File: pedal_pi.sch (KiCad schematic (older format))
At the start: 20 parts

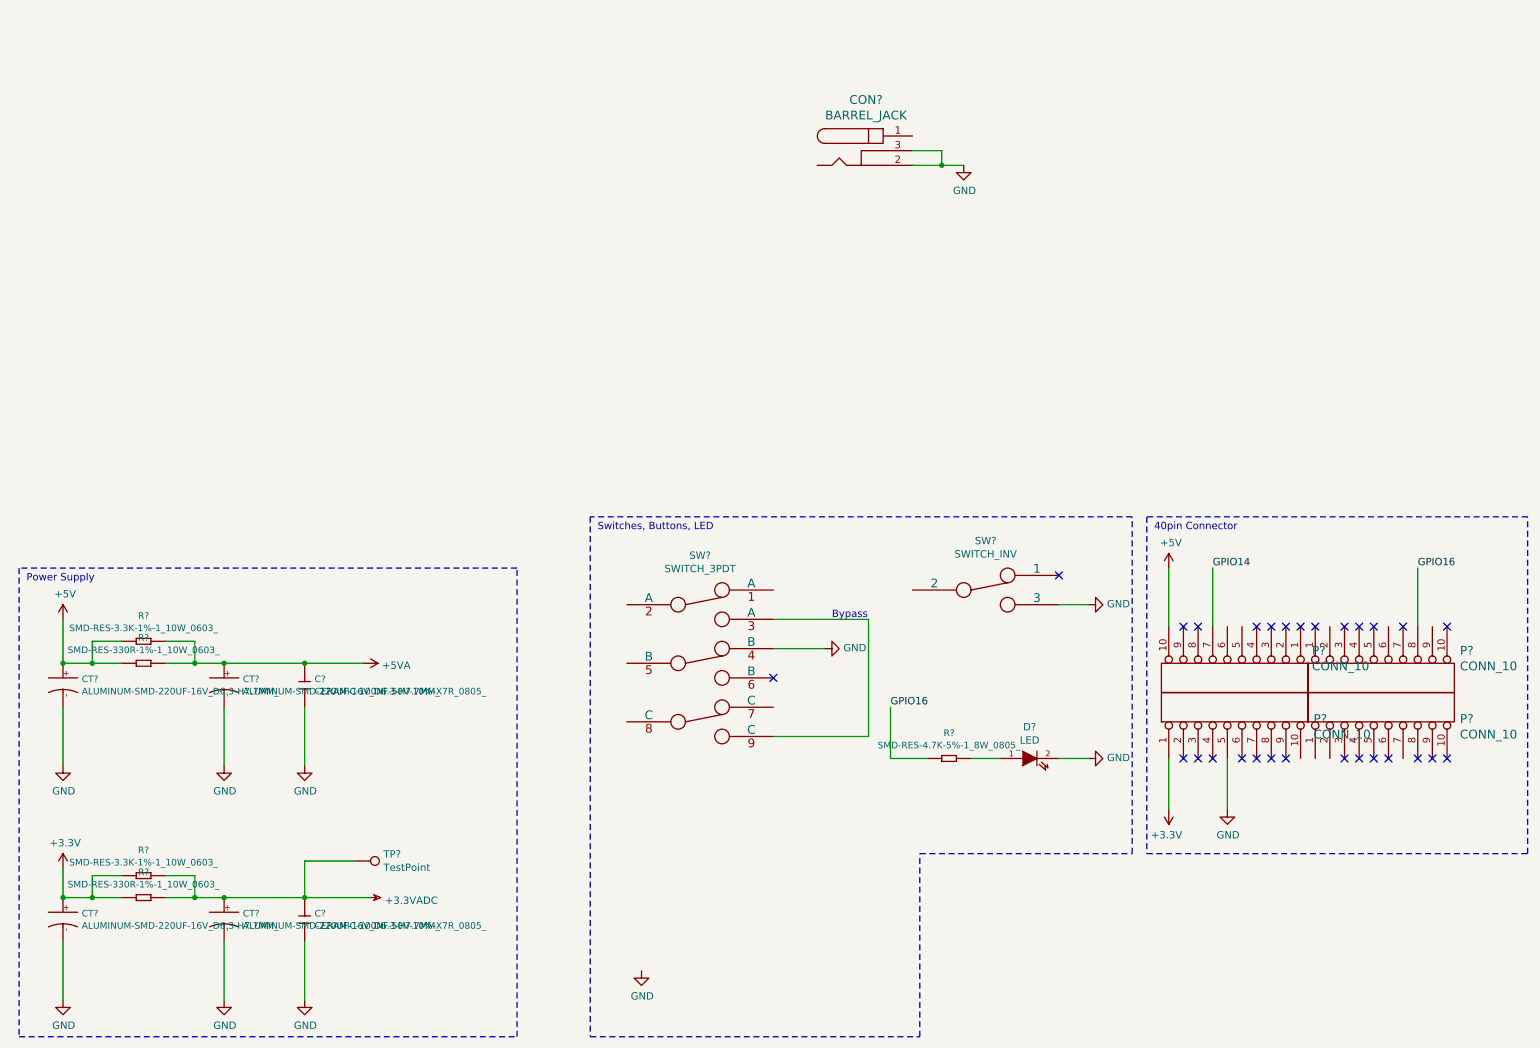
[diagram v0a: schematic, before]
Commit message: added more components to schematic, but stuck on what component to use for dipole ceramic capacitor. List of components that has to be self sourced is placed in the README.md
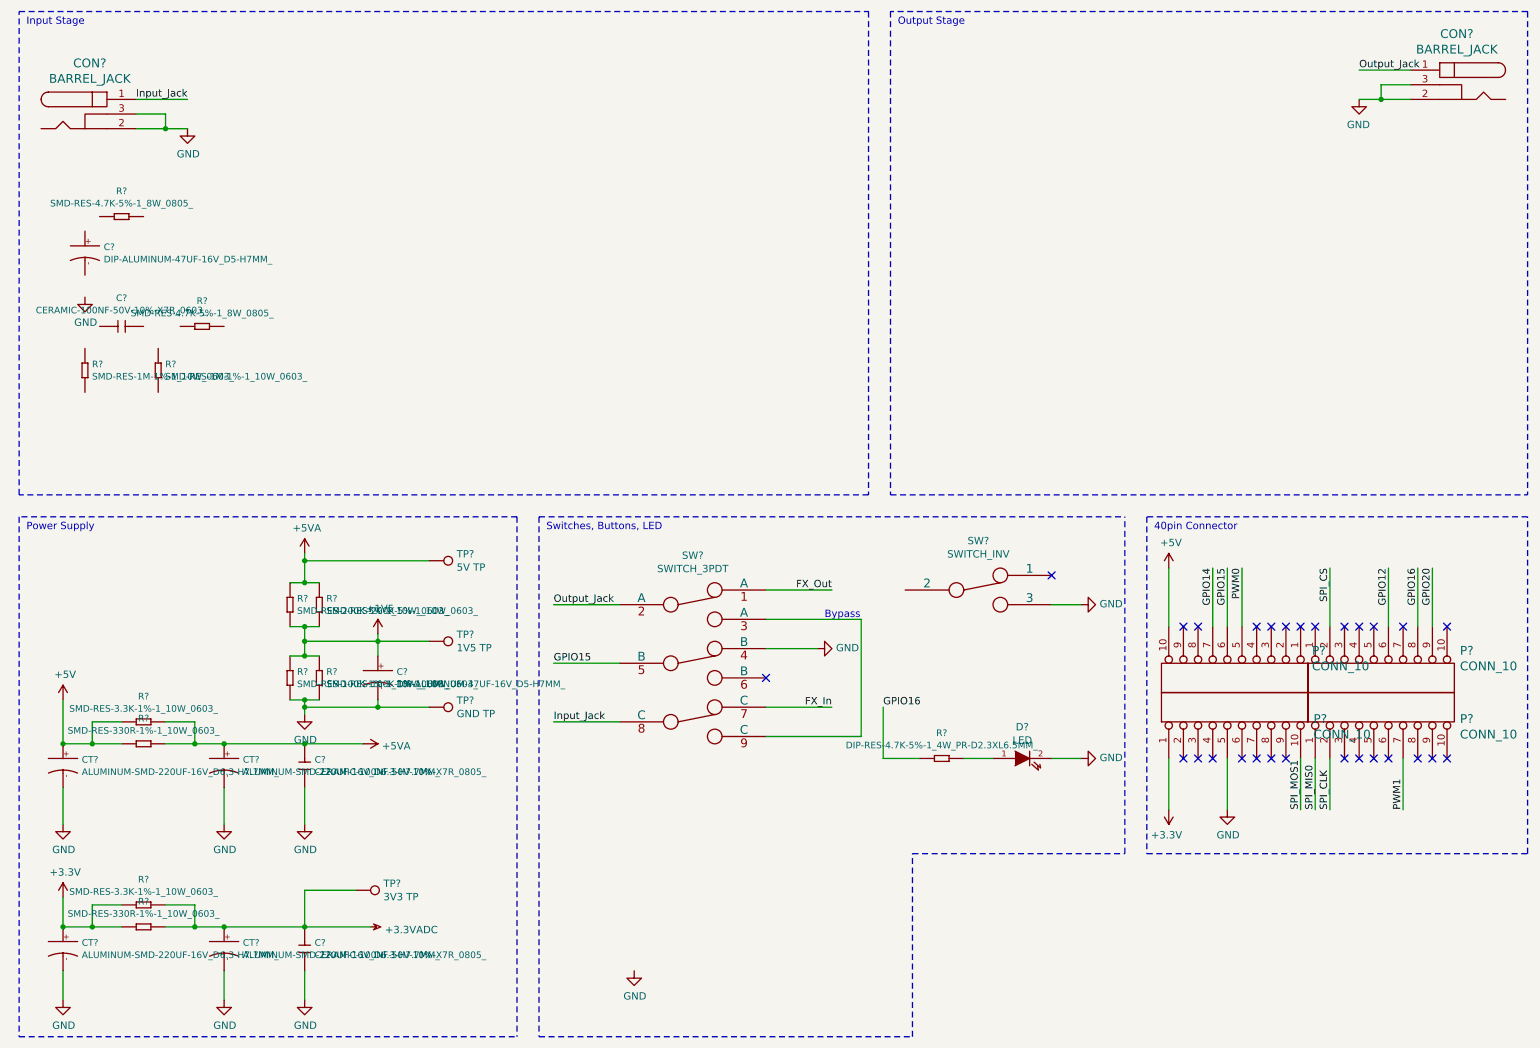
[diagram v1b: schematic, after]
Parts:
- removed R?: SMD-RES-4.7K-5%-1_8W_0805_, symbol OPL_Resistor:SMD-RES-4.7K-5%-1_8W_0805_
- added C?: CERAMIC-100NF-50V-10%-X7R_0603_, symbol OPL_Capacitor:CERAMIC-100NF-50V-10%-X7R_0603_
- added C? (x2): DIP-ALUMINUM-47UF-16V_D5-H7MM_, symbol OPL_Capacitor:DIP-ALUMINUM-47UF-16V_D5-H7MM_
- added CON?: BARREL_JACK, symbol pedal-pi-libs:BARREL_JACK
- added R?: DIP-RES-4.7K-5%-1_4W_PR-D2.3XL6.5MM_, symbol OPL_Resistor:DIP-RES-4.7K-5%-1_4W_PR-D2.3XL6.5MM_
- added R? (x2): SMD-RES-1M-1%-1_10W_0603_, symbol OPL_Resistor:SMD-RES-1M-1%-1_10W_0603_
- added R? (x2): SMD-RES-4.7K-5%-1_8W_0805_, symbol OPL_Resistor:SMD-RES-4.7K-5%-1_8W_0805_
- added R? (x2): SMD-RES-100K-1%-1_10W_0603_, symbol OPL_Resistor:SMD-RES-100K-1%-1_10W_0603_
- added R? (x2): SMD-RES-200K-5%-1_10W_0603_, symbol OPL_Resistor:SMD-RES-200K-5%-1_10W_0603_
- added TP?: 1V5 TP, symbol Connector:TestPoint
- added TP?: GND TP, symbol Connector:TestPoint
- added TP?: 5V TP, symbol Connector:TestPoint
- TP?: value TestPoint -> 3V3 TP
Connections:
- net +5VA: now also R?.1, R?.1, TP?.1
- net GND: now also C?.-, CON?.2, CON?.3, R?.2, R?.2, TP?.1
- net GPIO16: now also R?.1
- net PWM0: now reaches P?.5 (P5)
- net GPIO15: now reaches P?.6 (P6)
- net GPIO15: now also SW?.5 (B)
- net SPI_CS: now reaches P?.2 (P2)
- net GPIO12: now reaches P?.6 (P6)
- net GPIO20: now reaches P?.9 (P9)
- net SPI_MIS0: now reaches P?.1 (P1)
- net SPI_CLK: now reaches P?.2 (P2)
- net PWM1: now reaches P?.7 (P7)
- net SPI_MOS1: now reaches P?.10 (P10)
- net FX_Out: now reaches SW?.1 (A)
- net Output_Jack: now reaches SW?.2 (A)
- net Output_Jack: now also CON?.1
- net FX_In: now reaches SW?.7 (C)
- net Input_Jack: now reaches SW?.8 (C)
- net Input_Jack: now also CON?.1
- net at D?.1 (A): now also R?.2
- new net +1V5: C?.+, R?.1, R?.1, R?.2, R?.2, TP?.1
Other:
- note added: "Input Stage\n"
- note added: "Output Stage\n"
- moved on the sheet: C?, CON?, CT?, D?, R?, SW?, TP?
